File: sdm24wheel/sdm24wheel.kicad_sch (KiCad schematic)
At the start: 50 parts, among them J1 JST_XH_3P, J2 Conn_ARM_SWD_TagConnect_TC2030, J3 USB_B_Micro, J4 JST_XH_4P, U1 STM32F405RGT6, U2 MLX90614, U3 MIC37100-3.3WS, U4 24LC01BT-E/LT, U5 SN65HVD230, U6 USBLC6-2SC6, Y1 12MHz

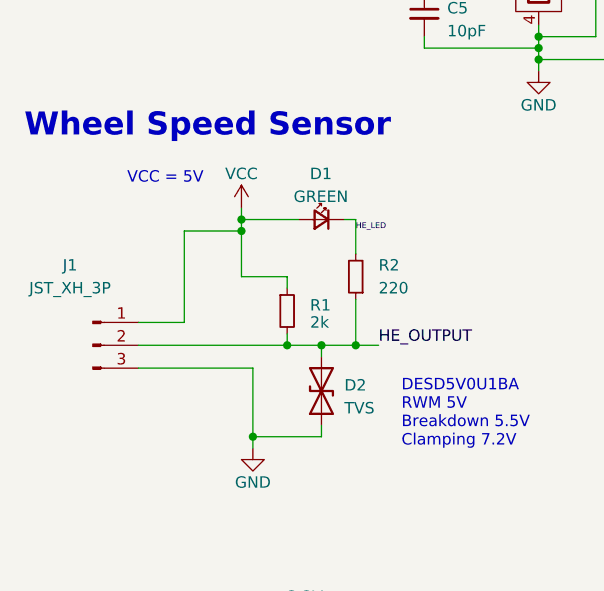
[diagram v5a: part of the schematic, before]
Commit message: wheel board updates
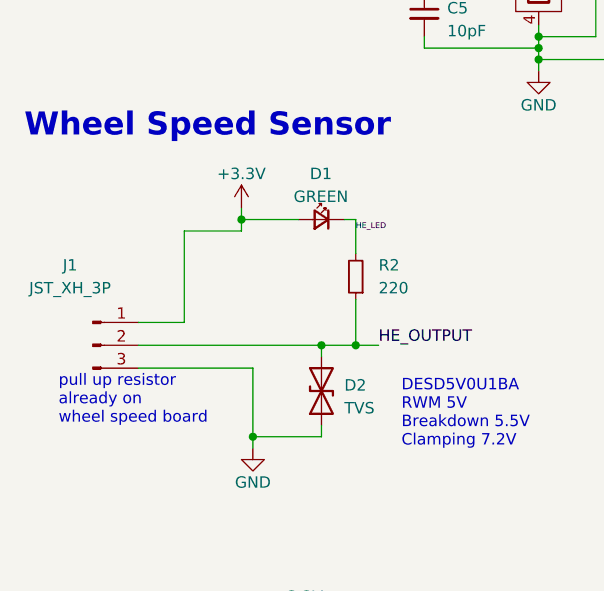
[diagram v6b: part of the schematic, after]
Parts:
- removed R1: 2k, Resistor_SMD:R_0805_2012Metric, symbol Device:R_Small
- D4: footprint Library:Dialight_561-XX0X-XXX -> LED_SMD:LED_0805_2012Metric
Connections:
- net +3.3V: now also D1.2 (A), J1.1 (Pin_1)
- net VCC: no longer D1.2 (A), J1.1 (Pin_1)
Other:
- note added: "pull up resistor already on wheel speed board"
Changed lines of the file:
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@@
   (title_block
     (title "SDM-24 Wheel Board")
-    (date "2023-09-04")
+    (date "2023-10-22")
     (rev "v1")
     (company "Sun Devil Motorsports")
@@
   (junction (at 186.69 83.82) (diameter 0) (color 0 0 0 0)
   )
-  (junction (at 39.37 111.76) (diameter 0) (color 0 0 0 0)
-  )
   (junction (at 91.44 27.94) (diameter 0) (color 0 0 0 0)
   )
@@
   )
   (junction (at 148.59 27.94) (diameter 0) (color 0 0 0 0)
-  )
-  (junction (at 44.45 124.46) (diameter 0) (color 0 0 0 0)
   )
   (junction (at 77.47 19.05) (diameter 0) (color 0 0 0 0)
@@
     (stroke (width 0) (type default))
   )
-  (wire (pts (xy 44.45 124.46) (xy 48.26 124.46))
+  (wire (pts (xy 27.94 124.46) (xy 48.26 124.46))
     (stroke (width 0) (type default))
   )
@@
     (stroke (width 0) (type default))
   )
-  (wire (pts (xy 39.37 116.84) (xy 44.45 116.84))
-    (stroke (width 0) (type default))
-  )
   (wire (pts (xy 102.87 107.95) (xy 102.87 105.41))
     (stroke (width 0) (type default))
@@
     (stroke (width 0) (type default))
   )
-  (wire (pts (xy 39.37 111.76) (xy 39.37 116.84))
-    (stroke (width 0) (type default))
-  )
   (wire (pts (xy 72.39 90.17) (xy 72.39 91.44))
     (stroke (width 0) (type default))
@@
     (stroke (width 0) (type default))
   )
-  (wire (pts (xy 27.94 124.46) (xy 44.45 124.46))
-    (stroke (width 0) (type default))
-  )
   (wire (pts (xy 170.18 26.67) (xy 170.18 29.21))
     (stroke (width 0) (type default))
@@
     (stroke (width 0) (type default))
   )
-  (wire (pts (xy 44.45 118.11) (xy 44.45 116.84))
-    (stroke (width 0) (type default))
-  )
   (wire (pts (xy 156.21 96.52) (xy 165.1 96.52))
     (stroke (width 0) (type default))
@@
   )
   (wire (pts (xy 93.98 113.03) (xy 93.98 114.3))
-    (stroke (width 0) (type default))
-  )
-  (wire (pts (xy 44.45 123.19) (xy 44.45 124.46))
     (stroke (width 0) (type default))
   )
@@
     (effects (font (size 1.27 1.27)) (justify left bottom))
   )
+  (text "pull up resistor\nalready on\nwheel speed board" (at 19.05 133.35 0)
+    (effects (font (size 1.27 1.27)) (justify left bottom))
+  )
   (text "STM32F405" (at 163.83 48.26 0)
     (effects (font (size 2.56 2.56) (thickness 0.512) bold) (justify left bottom))
@@
   )
   (text "ECS-120-10-36Q-AES-TR" (at 50.8 74.93 0)
-    (effects (font (size 1.27 1.27)) (justify left bottom))
-  )
-  (text "VCC = 5V\n" (at 26.67 106.68 0)
     (effects (font (size 1.27 1.27)) (justify left bottom))
   )
@@
     )
   )
-  (symbol (lib_id "Device:R_Small") (at 44.45 120.65 0) (unit 1)
-    (in_bom yes) (on_board yes) (dnp no)
-    (property "Reference" "R1" (at 46.99 120.015 0)
-      (effects (font (size 1.27 1.27)) (justify left))
-    )
-    (property "Value" "2k" (at 46.99 121.92 0)
-      (effects (font (size 1.27 1.27)) (justify left))
-    )
-    (property "Footprint" "Resistor_SMD:R_0805_2012Metric" (at 44.45 120.65 0)
-      (effects (font (size 1.27 1.27)) hide)
-    )
-    (property "Datasheet" "~" (at 44.45 120.65 0)
-      (effects (font (size 1.27 1.27)) hide)
-    )
-    (pin "1")
-    (pin "2")
-    (instances
-      (project "sdm24wheel"
-        (path "/58bd889d-28e2-49da-85df-8e04b7f08117"
-          (reference "R1") (unit 1)
-        )
-      )
-    )
-  )
   (symbol (lib_id "Device:C_Small") (at 186.69 80.01 0) (unit 1)
     (in_bom yes) (on_board yes) (dnp no) (fields_autoplaced)
@@
         (path "/58bd889d-28e2-49da-85df-8e04b7f08117"
           (reference "C6") (unit 1)
+        )
+      )
+    )
+  )
+  (symbol (lib_id "power:+3.3V") (at 39.37 109.22 0) (unit 1)
+    (in_bom yes) (on_board yes) (dnp no) (fields_autoplaced)
+    (property "Reference" "#PWR03" (at 39.37 113.03 0)
+      (effects (font (size 1.27 1.27)) hide)
+    )
+    (property "Value" "+3.3V" (at 39.37 105.41 0)
+      (effects (font (size 1.27 1.27)))
+    )
+    (property "Footprint" "" (at 39.37 109.22 0)
+      (effects (font (size 1.27 1.27)) hide)
+    )
+    (property "Datasheet" "" (at 39.37 109.22 0)
+      (effects (font (size 1.27 1.27)) hide)
+    )
+    (pin "1")
+    (instances
+      (project "sdm24wheel"
+        (path "/58bd889d-28e2-49da-85df-8e04b7f08117"
+          (reference "#PWR03") (unit 1)
         )
       )
@@
     )
   )
-  (symbol (lib_id "power:VCC") (at 39.37 109.22 0) (unit 1)
-    (in_bom yes) (on_board yes) (dnp no) (fields_autoplaced)
-    (property "Reference" "#PWR03" (at 39.37 113.03 0)
-      (effects (font (size 1.27 1.27)) hide)
-    )
-    (property "Value" "VCC" (at 39.37 105.41 0)
-      (effects (font (size 1.27 1.27)))
-    )
-    (property "Footprint" "" (at 39.37 109.22 0)
-      (effects (font (size 1.27 1.27)) hide)
-    )
-    (property "Datasheet" "" (at 39.37 109.22 0)
-      (effects (font (size 1.27 1.27)) hide)
-    )
-    (pin "1")
-    (instances
-      (project "sdm24wheel"
-        (path "/58bd889d-28e2-49da-85df-8e04b7f08117"
-          (reference "#PWR03") (unit 1)
-        )
-      )
-    )
-  )
   (symbol (lib_id "Device:R_Small") (at 224.79 83.82 0) (unit 1)
     (in_bom yes) (on_board yes) (dnp no) (fields_autoplaced)
@@
       (effects (font (size 1.27 1.27)))
     )
-    (property "Footprint" "Library:Dialight_561-XX0X-XXX" (at 173.99 81.28 90)
-      (effects (font (size 1.27 1.27)) hide)
-    )
+    (property "Footprint" "LED_SMD:LED_0805_2012Metric" (at 173.99 81.28 90)
+      (effects (font (size 1.27 1.27)) hide)
+    )

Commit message: finalize wheel board
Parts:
- renumbered R2 to R1, R3 to R2, R5 to R3, R7 to R4, R6 to R5, R8 to R6, R9 to R7, R10 to R8

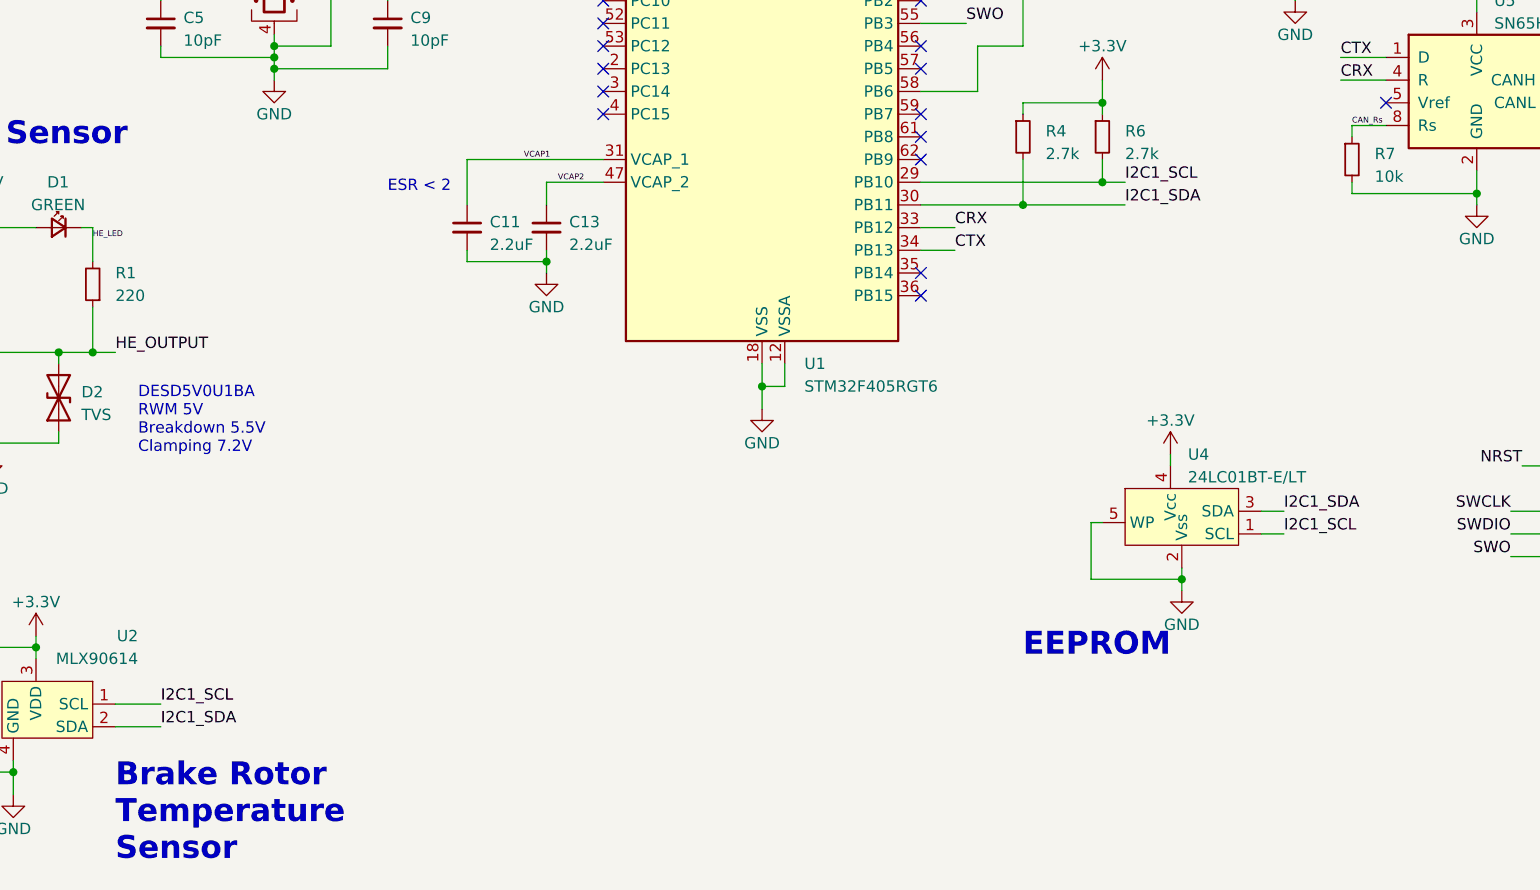
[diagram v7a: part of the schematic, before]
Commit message: update label wheel board
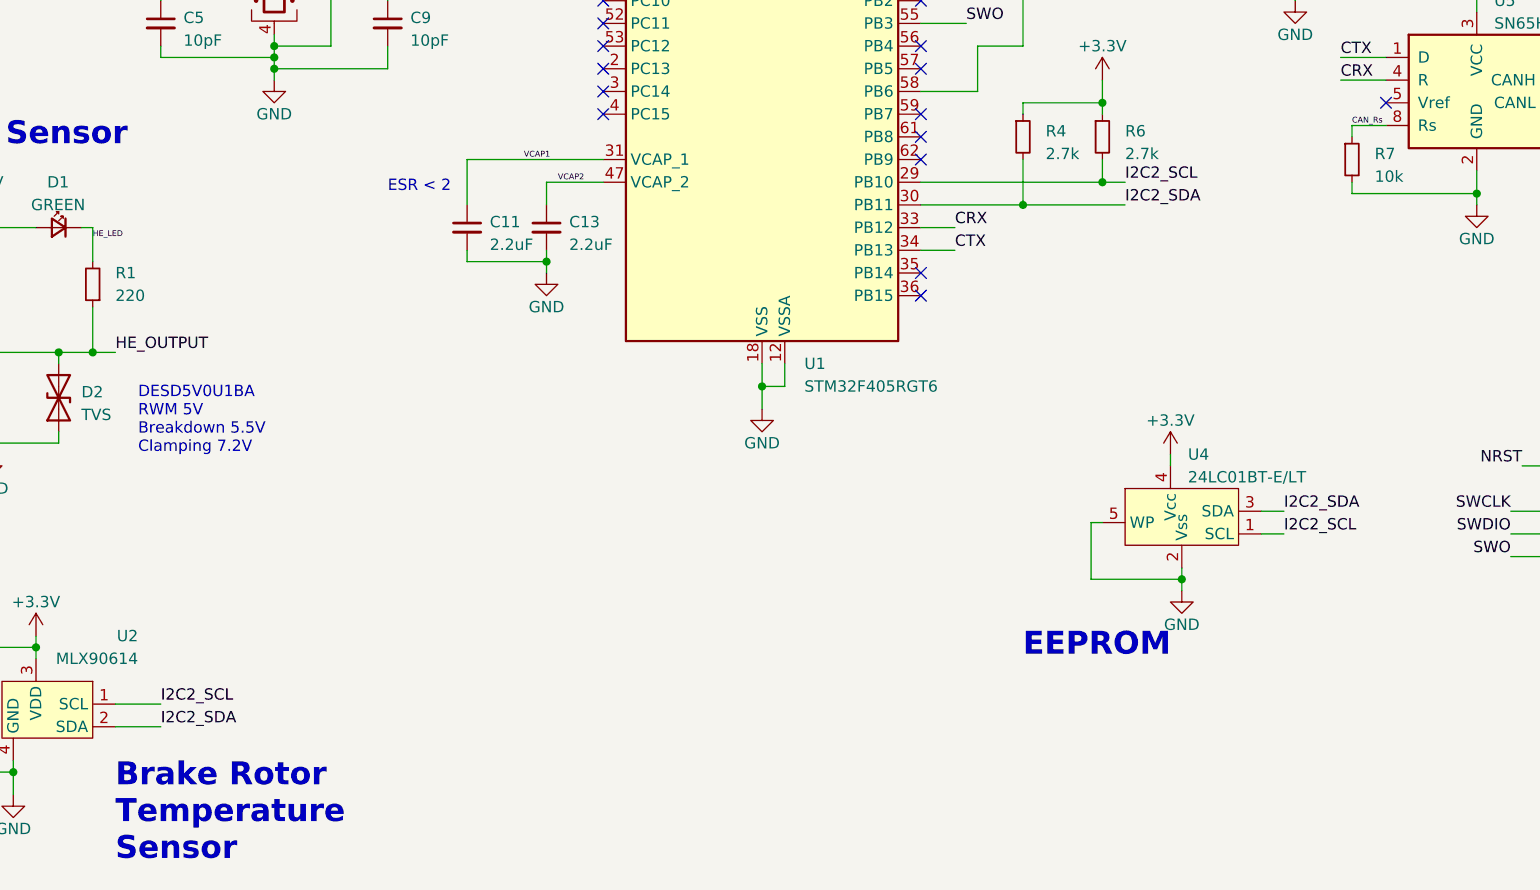
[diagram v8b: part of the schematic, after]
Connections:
- net I2C1_SCL renamed I2C2_SCL
- net I2C1_SDA renamed I2C2_SDA
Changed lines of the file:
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@@
     (effects (font (size 1.27 1.27)) (justify left bottom))
   )
-  (label "I2C1_SDA" (at 185.42 142.24 0) (fields_autoplaced)
+  (label "I2C2_SDA" (at 185.42 142.24 0) (fields_autoplaced)
     (effects (font (size 1.27 1.27)) (justify left bottom))
   )
@@
     (effects (font (size 1.27 1.27)) (justify right bottom))
   )
-  (label "I2C1_SDA" (at 167.64 107.95 0) (fields_autoplaced)
+  (label "I2C2_SDA" (at 167.64 107.95 0) (fields_autoplaced)
     (effects (font (size 1.27 1.27)) (justify left bottom))
   )
@@
     (effects (font (size 1.27 1.27)) (justify left bottom))
   )
-  (label "I2C1_SCL" (at 59.69 163.83 0) (fields_autoplaced)
+  (label "I2C2_SCL" (at 59.69 163.83 0) (fields_autoplaced)
     (effects (font (size 1.27 1.27)) (justify left bottom))
   )
@@
     (effects (font (size 1.27 1.27)) (justify right bottom))
   )
-  (label "I2C1_SDA" (at 59.69 166.37 0) (fields_autoplaced)
+  (label "I2C2_SDA" (at 59.69 166.37 0) (fields_autoplaced)
     (effects (font (size 1.27 1.27)) (justify left bottom))
   )
@@
     (effects (font (size 1.27 1.27)) (justify right bottom))
   )
-  (label "I2C1_SCL" (at 167.64 105.41 0) (fields_autoplaced)
+  (label "I2C2_SCL" (at 167.64 105.41 0) (fields_autoplaced)
     (effects (font (size 1.27 1.27)) (justify left bottom))
   )
@@
     (effects (font (size 1.27 1.27)) (justify left bottom))
   )
-  (label "I2C1_SCL" (at 185.42 144.78 0) (fields_autoplaced)
+  (label "I2C2_SCL" (at 185.42 144.78 0) (fields_autoplaced)
     (effects (font (size 1.27 1.27)) (justify left bottom))
   )
